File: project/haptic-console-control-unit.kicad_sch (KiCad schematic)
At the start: 30 parts, among them J1 JST-XH-5, J2 JST-XH-5, U1 Teensy 4.1

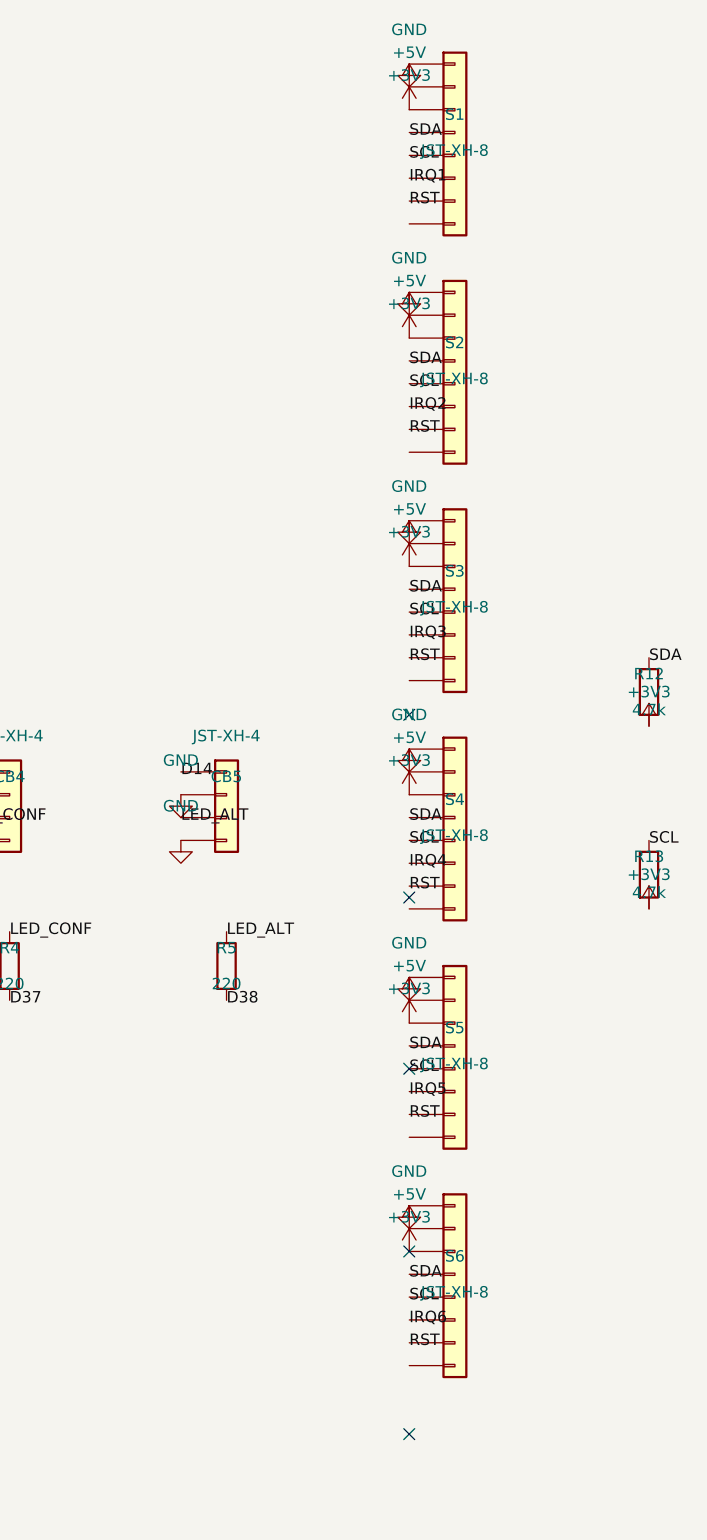
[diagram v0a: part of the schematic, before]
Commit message: S1-S6: swap 8-pin JST-XH-8 to 6-pin JST-XH-6, drop RST, match 6P standard pinout
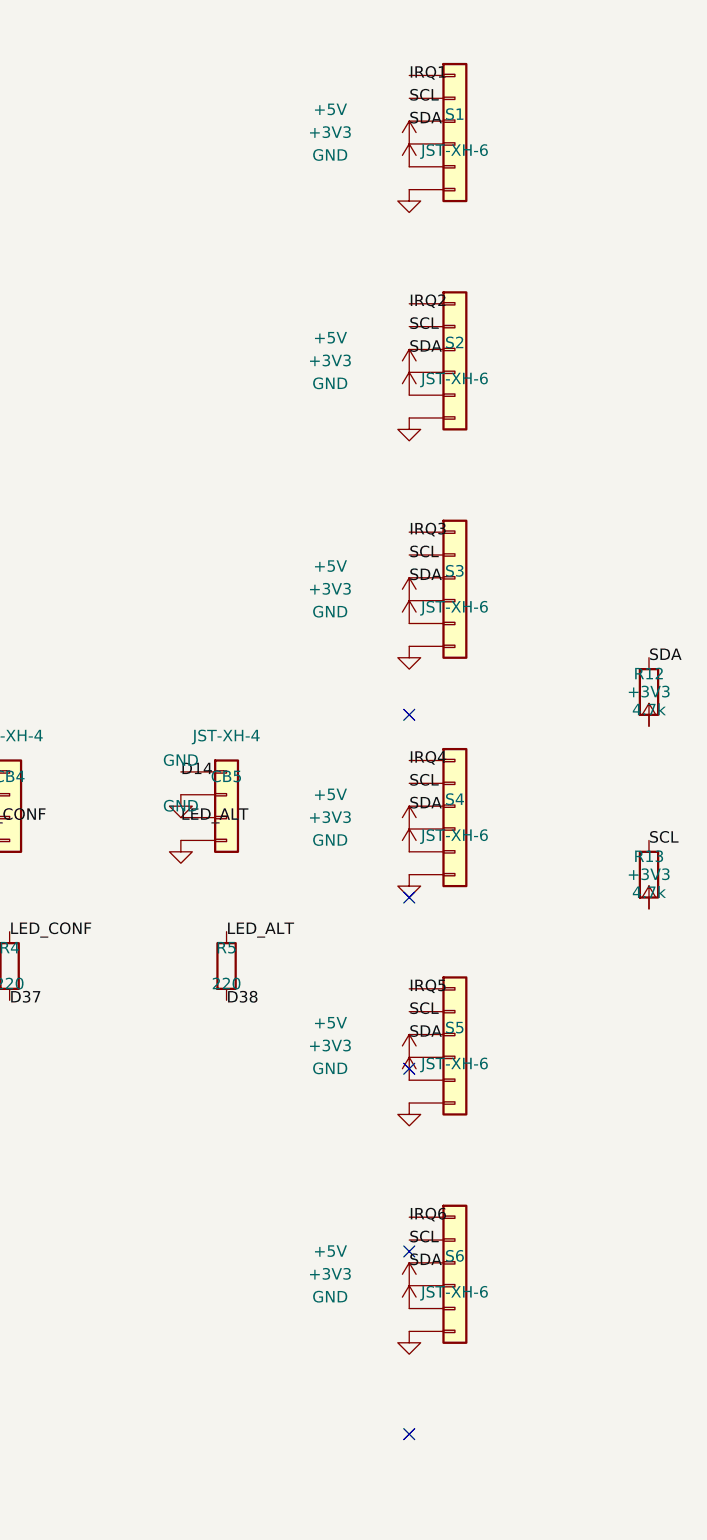
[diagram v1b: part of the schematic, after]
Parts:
- S1, S2, S3, S4, S5, S6: value JST-XH-8 -> JST-XH-6; footprint Connector_JST:JST_XH_B8B-XH-A_1x08_P2.50mm_Vertical -> Connector_JST:JST_XH_B6B-XH-A_1x06_P2.50mm_Vertical; symbol Connector_Generic:Conn_01x08 -> Connector_Generic:Conn_01x06
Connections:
- net +3V3: now also S1.5 (Pin_5), S2.5 (Pin_5), S3.5 (Pin_5), S4.5 (Pin_5), S5.5 (Pin_5), S6.5 (Pin_5); no longer S1.3 (Pin_3), S2.3 (Pin_3), S3.3 (Pin_3), S4.3 (Pin_3), S5.3 (Pin_3), S6.3 (Pin_3)
- net +5V: now also S1.4 (Pin_4), S2.4 (Pin_4), S3.4 (Pin_4), S4.4 (Pin_4), S5.4 (Pin_4), S6.4 (Pin_4); no longer S1.2 (Pin_2), S2.2 (Pin_2), S3.2 (Pin_2), S4.2 (Pin_2), S5.2 (Pin_2), S6.2 (Pin_2)
- net GND: now also S1.6 (Pin_6), S2.6 (Pin_6), S3.6 (Pin_6), S4.6 (Pin_6), S5.6 (Pin_6), S6.6 (Pin_6); no longer S1.1 (Pin_1), S2.1 (Pin_1), S3.1 (Pin_1), S4.1 (Pin_1), S5.1 (Pin_1), S6.1 (Pin_1)
- net IRQ1: now also S1.1 (Pin_1); no longer S1.6 (Pin_6)
- net IRQ2: now also S2.1 (Pin_1); no longer S2.6 (Pin_6)
- net IRQ3: now also S3.1 (Pin_1); no longer S3.6 (Pin_6)
- net IRQ4: now also S4.1 (Pin_1); no longer S4.6 (Pin_6)
- net IRQ5: now also S5.1 (Pin_1); no longer S5.6 (Pin_6)
- net IRQ6: now also S6.1 (Pin_1); no longer S6.6 (Pin_6)
- net SCL: now also S1.2 (Pin_2), S2.2 (Pin_2), S3.2 (Pin_2), S4.2 (Pin_2), S5.2 (Pin_2), S6.2 (Pin_2); no longer S1.5 (Pin_5), S2.5 (Pin_5), S3.5 (Pin_5), S4.5 (Pin_5), S5.5 (Pin_5), S6.5 (Pin_5)
- net SDA: now also S1.3 (Pin_3), S2.3 (Pin_3), S3.3 (Pin_3), S4.3 (Pin_3), S5.3 (Pin_3), S6.3 (Pin_3); no longer S1.4 (Pin_4), S2.4 (Pin_4), S3.4 (Pin_4), S4.4 (Pin_4), S5.4 (Pin_4), S6.4 (Pin_4)
- removed net RST: S1.7 (Pin_7), S2.7 (Pin_7), S3.7 (Pin_7), S4.7 (Pin_7), S5.7 (Pin_7), S6.7 (Pin_7)
